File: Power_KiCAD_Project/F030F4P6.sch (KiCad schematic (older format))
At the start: 11 parts, among them IC1 STM32L562VET6Q, Y1 Crystal

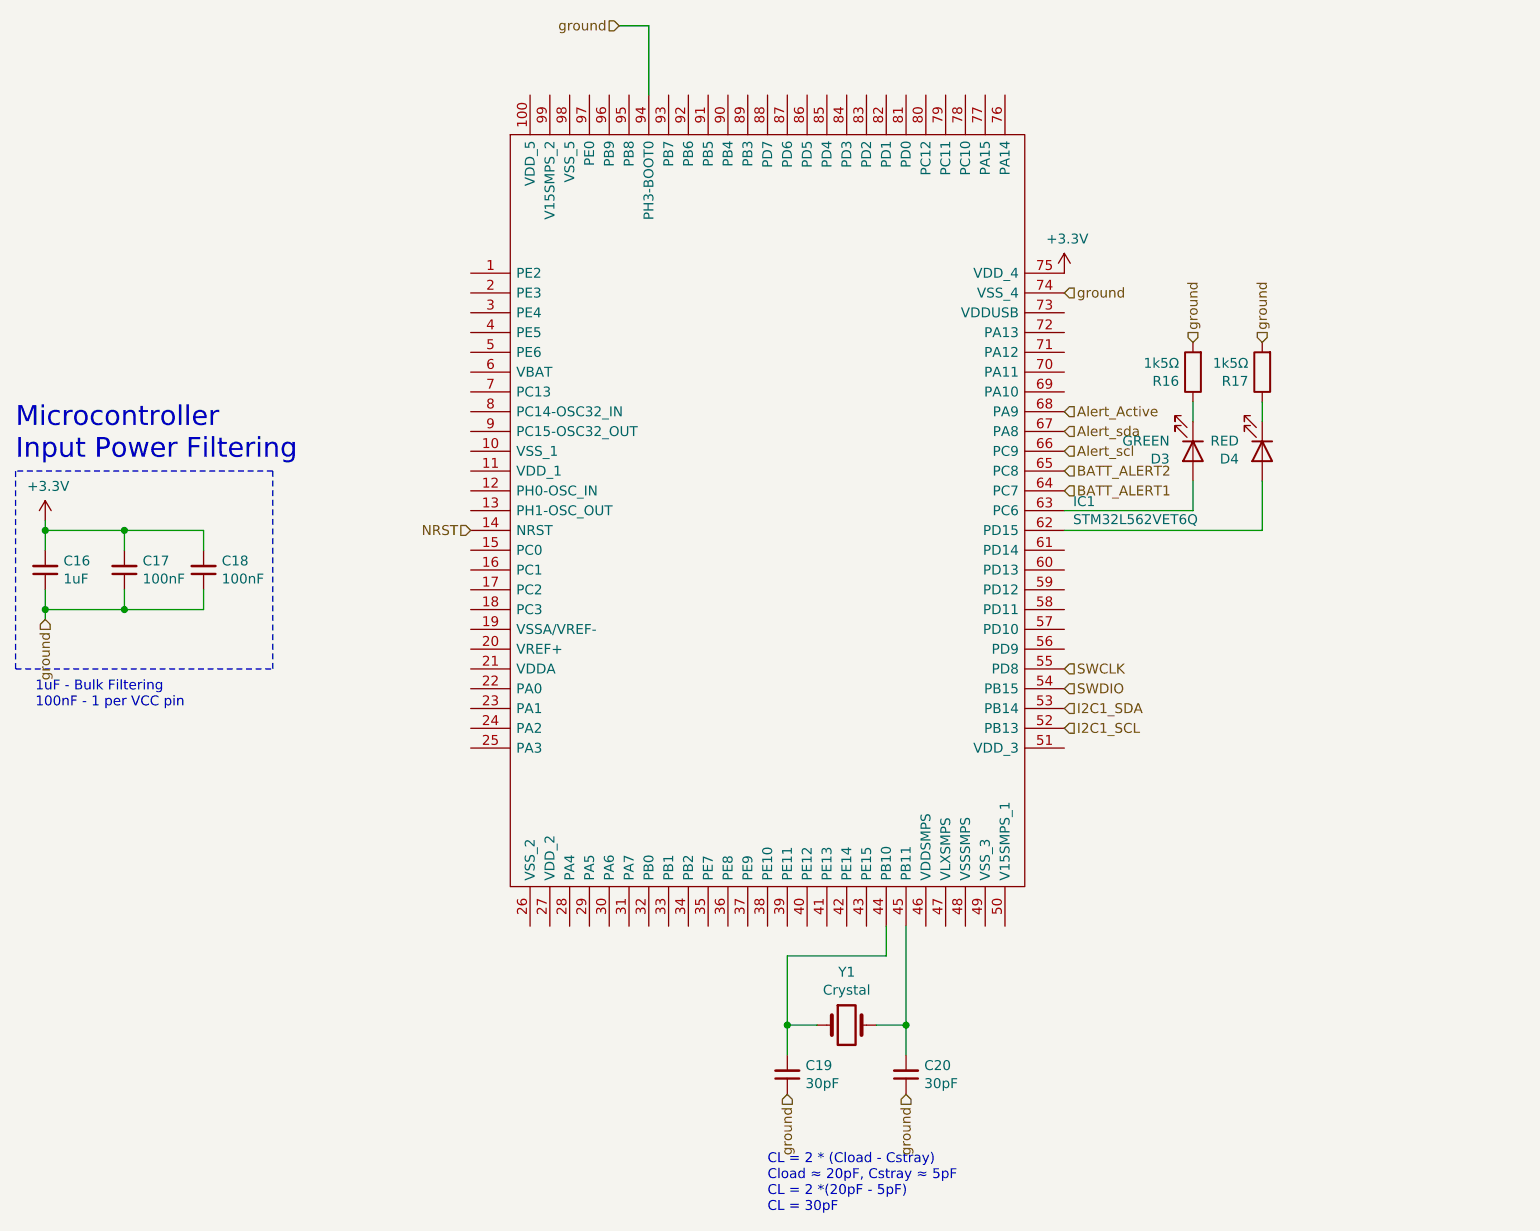
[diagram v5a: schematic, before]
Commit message: Changes to PCB
re did the pcb and added a "switch"
basically its just an xt60 connector in series with the other ones that needs to be shorted for the board to get power
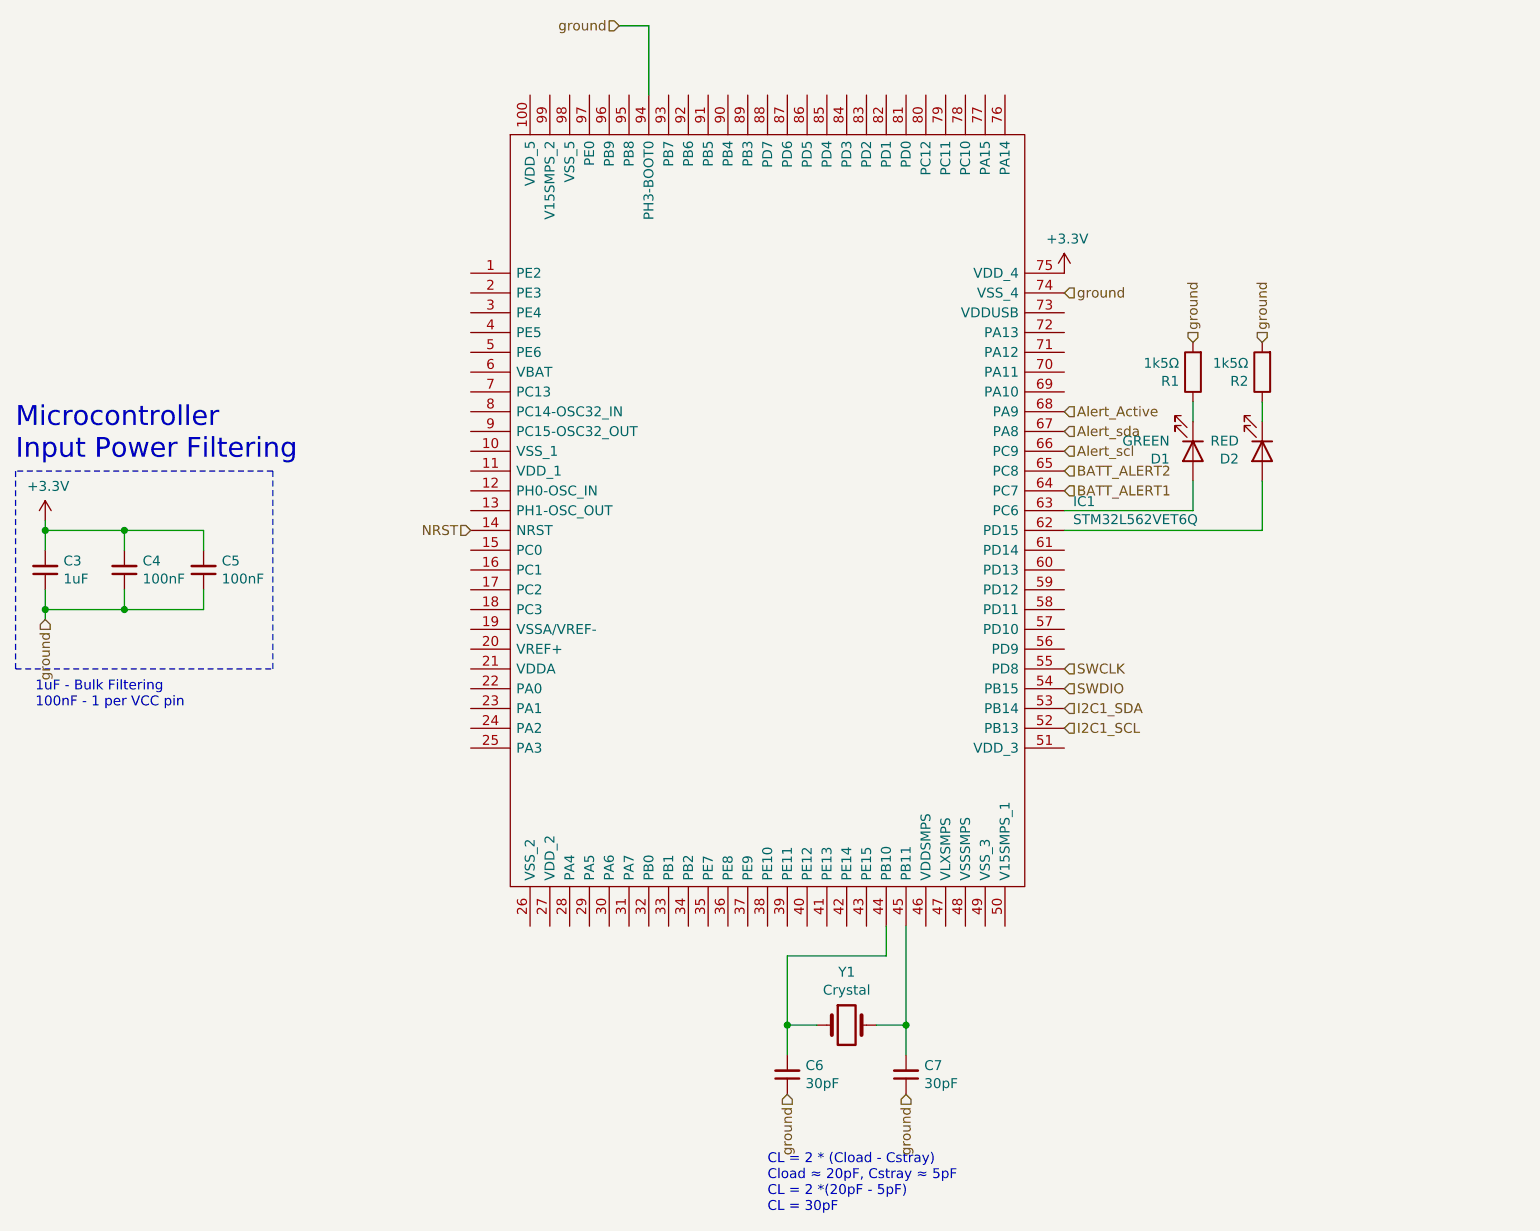
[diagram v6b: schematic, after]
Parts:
- renumbered C16 to C3, C17 to C4, C18 to C5, C19 to C6, C20 to C7, D3 to D1, D4 to D2, R16 to R1, R17 to R2
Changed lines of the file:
@@
 P 1700 4050
 AR Path="/61614678" Ref="C?"  Part="1"
-AR Path="/6160DF75/61614678" Ref="C16"  Part="1"
-F 0 "C16" H 1608 4004 50  0000 R CNN
+AR Path="/6160DF75/61614678" Ref="C3"  Part="1"
+F 0 "C3" H 1608 4004 50  0000 R CNN
 F 1 "1uF" H 1608 4095 50  0000 R CNN
 F 2 "Capacitor_SMD:C_0603_1608Metric" H 1700 4050 50  0001 C CNN
@@
 P 2100 4050
 AR Path="/6161467E" Ref="C?"  Part="1"
-AR Path="/6160DF75/6161467E" Ref="C17"  Part="1"
-F 0 "C17" H 2008 4004 50  0000 R CNN
+AR Path="/6160DF75/6161467E" Ref="C4"  Part="1"
+F 0 "C4" H 2008 4004 50  0000 R CNN
 F 1 "100nF" H 2008 4095 50  0000 R CNN
 F 2 "Capacitor_SMD:C_0603_1608Metric" H 2100 4050 50  0001 C CNN
@@
 P 2500 4050
 AR Path="/61614684" Ref="C?"  Part="1"
-AR Path="/6160DF75/61614684" Ref="C18"  Part="1"
-F 0 "C18" H 2408 4004 50  0000 R CNN
+AR Path="/6160DF75/61614684" Ref="C5"  Part="1"
+F 0 "C5" H 2408 4004 50  0000 R CNN
 F 1 "100nF" H 2408 4095 50  0000 R CNN
 F 2 "Capacitor_SMD:C_0603_1608Metric" H 2500 4050 50  0001 C CNN
@@
 P 1700 3800
 AR Path="/61614698" Ref="#PWR?"  Part="1"
-AR Path="/6160DF75/61614698" Ref="#PWR018"  Part="1"
-F 0 "#PWR018" H 1700 3650 50  0001 C CNN
+AR Path="/6160DF75/61614698" Ref="#PWR06"  Part="1"
+F 0 "#PWR06" H 1700 3650 50  0001 C CNN
 F 1 "+3.3V" H 1715 3973 50  0000 C CNN
 F 2 "" H 1700 3800 50  0001 C CNN
@@
 P 7850 3050
 AR Path="/616146C6" Ref="R?"  Part="1"
-AR Path="/6160DF75/616146C6" Ref="R17"  Part="1"
-F 0 "R17" H 7920 3096 50  0000 L CNN
+AR Path="/6160DF75/616146C6" Ref="R2"  Part="1"
+F 0 "R2" H 7920 3096 50  0000 L CNN
 F 1 "1k5Ω" H 7920 3005 50  0000 L CNN
 F 2 "Resistor_SMD:R_0603_1608Metric" V 7780 3050 50  0001 C CNN
@@
 P 7850 3450
 AR Path="/616146C0" Ref="D?"  Part="1"
-AR Path="/6160DF75/616146C0" Ref="D4"  Part="1"
-F 0 "D4" V 7889 3332 50  0000 R CNN
+AR Path="/6160DF75/616146C0" Ref="D2"  Part="1"
+F 0 "D2" V 7889 3332 50  0000 R CNN
 F 1 "RED" V 7798 3332 50  0000 R CNN
 F 2 "LED_SMD:LED_0603_1608Metric" H 7850 3450 50  0001 C CNN
@@
 P 7500 3450
 AR Path="/616146BA" Ref="D?"  Part="1"
-AR Path="/6160DF75/616146BA" Ref="D3"  Part="1"
-F 0 "D3" V 7539 3332 50  0000 R CNN
+AR Path="/6160DF75/616146BA" Ref="D1"  Part="1"
+F 0 "D1" V 7539 3332 50  0000 R CNN
 F 1 "GREEN" V 7448 3332 50  0000 R CNN
 F 2 "LED_SMD:LED_0603_1608Metric" H 7500 3450 50  0001 C CNN
@@
 P 7500 3050
 AR Path="/616146AE" Ref="R?"  Part="1"
-AR Path="/6160DF75/616146AE" Ref="R16"  Part="1"
-F 0 "R16" H 7570 3096 50  0000 L CNN
+AR Path="/6160DF75/616146AE" Ref="R1"  Part="1"
+F 0 "R1" H 7570 3096 50  0000 L CNN
 F 1 "1k5Ω" H 7570 3005 50  0000 L CNN
 F 2 "Resistor_SMD:R_0603_1608Metric" V 7430 3050 50  0001 C CNN
@@
 P 6850 2550
 AR Path="/6161463B" Ref="#PWR?"  Part="1"
-AR Path="/6160DF75/6161463B" Ref="#PWR019"  Part="1"
-F 0 "#PWR019" H 6850 2400 50  0001 C CNN
+AR Path="/6160DF75/6161463B" Ref="#PWR07"  Part="1"
+F 0 "#PWR07" H 6850 2400 50  0001 C CNN
 F 1 "+3.3V" H 6865 2723 50  0000 C CNN
 F 2 "" H 6850 2550 50  0001 C CNN
@@
 P 6050 6600
 AR Path="/61614648" Ref="C?"  Part="1"
-AR Path="/6160DF75/61614648" Ref="C20"  Part="1"
-F 0 "C20" H 5958 6554 50  0000 R CNN
+AR Path="/6160DF75/61614648" Ref="C7"  Part="1"
+F 0 "C7" H 5958 6554 50  0000 R CNN
 F 1 "30pF" H 5958 6645 50  0000 R CNN
 F 2 "Capacitor_SMD:C_0603_1608Metric" H 6050 6600 50  0001 C CNN
@@
 P 5450 6600
 AR Path="/6161464E" Ref="C?"  Part="1"
-AR Path="/6160DF75/6161464E" Ref="C19"  Part="1"
-F 0 "C19" H 5358 6554 50  0000 R CNN
+AR Path="/6160DF75/6161464E" Ref="C6"  Part="1"
+F 0 "C6" H 5358 6554 50  0000 R CNN
 F 1 "30pF" H 5358 6645 50  0000 R CNN
 F 2 "Capacitor_SMD:C_0603_1608Metric" H 5450 6600 50  0001 C CNN
